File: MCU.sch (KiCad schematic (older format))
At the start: 34 parts, among them Q1 BSS138, SW1 SW_Push, U2 STM32F722RETx

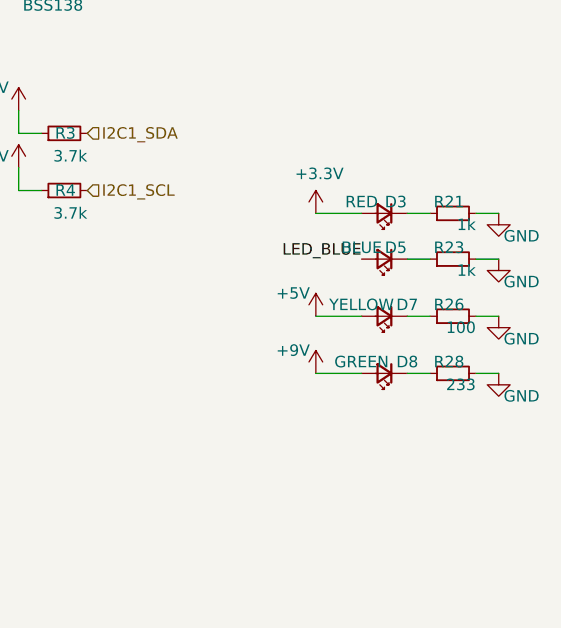
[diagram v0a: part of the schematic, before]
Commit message: Added LED for VCC
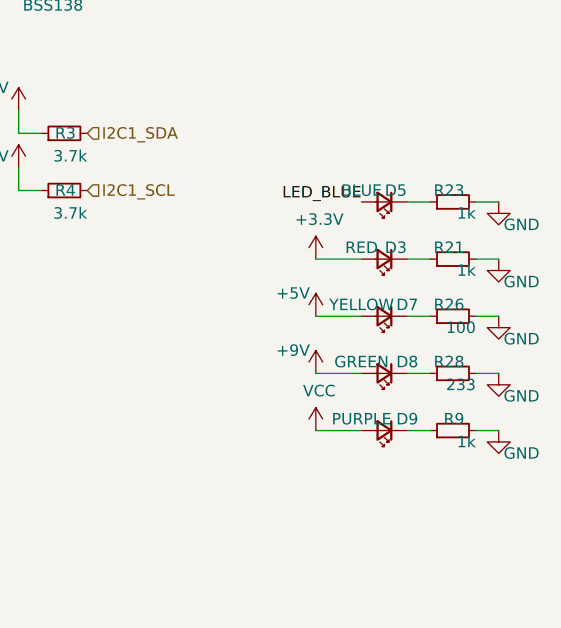
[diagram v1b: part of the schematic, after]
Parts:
- added D9: PURPLE, LED_SMD:LED_0603_1608Metric, symbol Device:LED_Small
- added R9: 1k, Resistor_SMD:R_0402_1005Metric, symbol Device:R_Small
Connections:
- net GND: now also R9.2
- net VCC: now also D9.2 (A)
- new net: D9.1 (K), R9.1
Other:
- moved on the sheet: D3, D5, R21, R23
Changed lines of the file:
@@
 $EndComp
+Wire Wire Line
+	7300 3300 7400 3300
+Wire Wire Line
+	7000 3300 7100 3300
 Wire Wire Line
 	7300 3550 7400 3550
 Wire Wire Line
 	7000 3550 7100 3550
-Wire Wire Line
-	7300 3350 7400 3350
-Wire Wire Line
-	7000 3350 7100 3350
 $Comp
 L power:GND #PWR031
 U 1 1 60863328
+P 7400 3300
+F 0 "#PWR031" H 7400 3050 50  0001 C CNN
+F 1 "GND" H 7500 3200 50  0000 C CNN
+F 2 "" H 7400 3300 50  0001 C CNN
+F 3 "" H 7400 3300 50  0001 C CNN
+	1    7400 3300
+	1    0    0    -1
+$EndComp
+$Comp
+L Device:R_Small R23
+U 1 1 6086332E
+P 7200 3300
+F 0 "R23" V 7250 3250 50  0000 L CNN
+F 1 "1k" V 7150 3200 50  0000 L CNN
+F 2 "Resistor_SMD:R_0402_1005Metric" H 7200 3300 50  0001 C CNN
+F 3 "~" H 7200 3300 50  0001 C CNN
+	1    7200 3300
+	0    -1   -1   0
+$EndComp
+$Comp
+L Device:LED_Small D5
+U 1 1 60863334
+P 6900 3300
+F 0 "D5" H 6850 3250 50  0000 C CNN
+F 1 "BLUE" H 7000 3250 50  0000 C CNN
+F 2 "LED_SMD:LED_0603_1608Metric" V 6900 3300 50  0001 C CNN
+F 3 "~" V 6900 3300 50  0001 C CNN
+	1    6900 3300
+	-1   0    0    1
+$EndComp
+NoConn ~ 4000 4950
+$Comp
+L power:GND #PWR030
+U 1 1 6086335B
 P 7400 3550
-F 0 "#PWR031" H 7400 3300 50  0001 C CNN
+F 0 "#PWR030" H 7400 3300 50  0001 C CNN
 F 1 "GND" H 7500 3450 50  0000 C CNN
 F 2 "" H 7400 3550 50  0001 C CNN
@@
 $EndComp
 $Comp
-L Device:R_Small R23
-U 1 1 6086332E
+L Device:R_Small R21
+U 1 1 60863361
 P 7200 3550
-F 0 "R23" V 7250 3500 50  0000 L CNN
+F 0 "R21" V 7250 3500 50  0000 L CNN
 F 1 "1k" V 7150 3450 50  0000 L CNN
 F 2 "Resistor_SMD:R_0402_1005Metric" H 7200 3550 50  0001 C CNN
@@
 $EndComp
 $Comp
-L Device:LED_Small D5
-U 1 1 60863334
+L Device:LED_Small D3
+U 1 1 60863367
 P 6900 3550
-F 0 "D5" H 6850 3500 50  0000 C CNN
-F 1 "BLUE" H 7000 3500 50  0000 C CNN
+F 0 "D3" H 6850 3500 50  0000 C CNN
+F 1 "RED" H 7000 3500 50  0000 C CNN
 F 2 "LED_SMD:LED_0603_1608Metric" V 6900 3550 50  0001 C CNN
 F 3 "~" V 6900 3550 50  0001 C CNN
 	1    6900 3550
-	-1   0    0    1
-$EndComp
-NoConn ~ 4000 4950
-$Comp
-L power:GND #PWR030
-U 1 1 6086335B
-P 7400 3350
-F 0 "#PWR030" H 7400 3100 50  0001 C CNN
-F 1 "GND" H 7500 3250 50  0000 C CNN
-F 2 "" H 7400 3350 50  0001 C CNN
-F 3 "" H 7400 3350 50  0001 C CNN
-	1    7400 3350
-	1    0    0    -1
-$EndComp
-$Comp
-L Device:R_Small R21
-U 1 1 60863361
-P 7200 3350
-F 0 "R21" V 7250 3300 50  0000 L CNN
-F 1 "1k" V 7150 3250 50  0000 L CNN
-F 2 "Resistor_SMD:R_0402_1005Metric" H 7200 3350 50  0001 C CNN
-F 3 "~" H 7200 3350 50  0001 C CNN
-	1    7200 3350
-	0    -1   -1   0
-$EndComp
-$Comp
-L Device:LED_Small D3
-U 1 1 60863367
-P 6900 3350
-F 0 "D3" H 6850 3300 50  0000 C CNN
-F 1 "RED" H 7000 3300 50  0000 C CNN
-F 2 "LED_SMD:LED_0603_1608Metric" V 6900 3350 50  0001 C CNN
-F 3 "~" V 6900 3350 50  0001 C CNN
-	1    6900 3350
 	-1   0    0    1
 $EndComp
@@
 L power:+3.3V #PWR029
 U 1 1 6086341E
-P 6600 3350
-F 0 "#PWR029" H 6600 3200 50  0001 C CNN
-F 1 "+3.3V" H 6615 3523 50  0000 C CNN
-F 2 "" H 6600 3350 50  0001 C CNN
-F 3 "" H 6600 3350 50  0001 C CNN
-	1    6600 3350
-	1    0    0    -1
-$EndComp
-Wire Wire Line
-	6600 3350 6800 3350
+P 6600 3550
+F 0 "#PWR029" H 6600 3400 50  0001 C CNN
+F 1 "+3.3V" H 6615 3723 50  0000 C CNN
+F 2 "" H 6600 3550 50  0001 C CNN
+F 3 "" H 6600 3550 50  0001 C CNN
+	1    6600 3550
+	1    0    0    -1
+$EndComp
+Wire Wire Line
+	6600 3550 6800 3550
 Connection ~ 3200 5750
 Connection ~ 3300 5750
@@
 Text HLabel 4000 2450 2    50   Input ~ 0
 LED
-Text Label 6800 3550 2    50   ~ 0
+Text Label 6800 3300 2    50   ~ 0
 LED_BLUE
 $Comp
@@
 USB_D+
 NoConn ~ 4000 4850
+Wire Wire Line
+	6600 4300 6800 4300
+Wire Wire Line
+	7300 4300 7400 4300
+Wire Wire Line
+	7000 4300 7100 4300
+$Comp
+L power:GND #PWR0178
+U 1 1 60A4CA89
+P 7400 4300
+F 0 "#PWR0178" H 7400 4050 50  0001 C CNN
+F 1 "GND" H 7500 4200 50  0000 C CNN
+F 2 "" H 7400 4300 50  0001 C CNN
+F 3 "" H 7400 4300 50  0001 C CNN
+	1    7400 4300
+	1    0    0    -1
+$EndComp
+$Comp
+L Device:R_Small R9
+U 1 1 60A4CA8F
+P 7200 4300
+F 0 "R9" V 7250 4250 50  0000 L CNN
+F 1 "1k" V 7150 4200 50  0000 L CNN
+F 2 "Resistor_SMD:R_0402_1005Metric" H 7200 4300 50  0001 C CNN
+F 3 "~" H 7200 4300 50  0001 C CNN
+	1    7200 4300
+	0    -1   -1   0
+$EndComp
+$Comp
+L Device:LED_Small D9
+U 1 1 60A4CA95
+P 6900 4300
+F 0 "D9" H 6800 4250 50  0000 C CNN
+F 1 "PURPLE" H 7000 4250 50  0000 C CNN
+F 2 "LED_SMD:LED_0603_1608Metric" V 6900 4300 50  0001 C CNN
+F 3 "~" V 6900 4300 50  0001 C CNN
+	1    6900 4300
+	-1   0    0    1
+$EndComp
+$Comp
+L power:VCC #PWR0179
+U 1 1 60A4FAC4
+P 6600 4300
+F 0 "#PWR0179" H 6600 4150 50  0001 C CNN
+F 1 "VCC" H 6615 4473 50  0000 C CNN
+F 2 "" H 6600 4300 50  0001 C CNN
+F 3 "" H 6600 4300 50  0001 C CNN
+	1    6600 4300
+	1    0    0    -1
+$EndComp
 $EndSCHEMATC

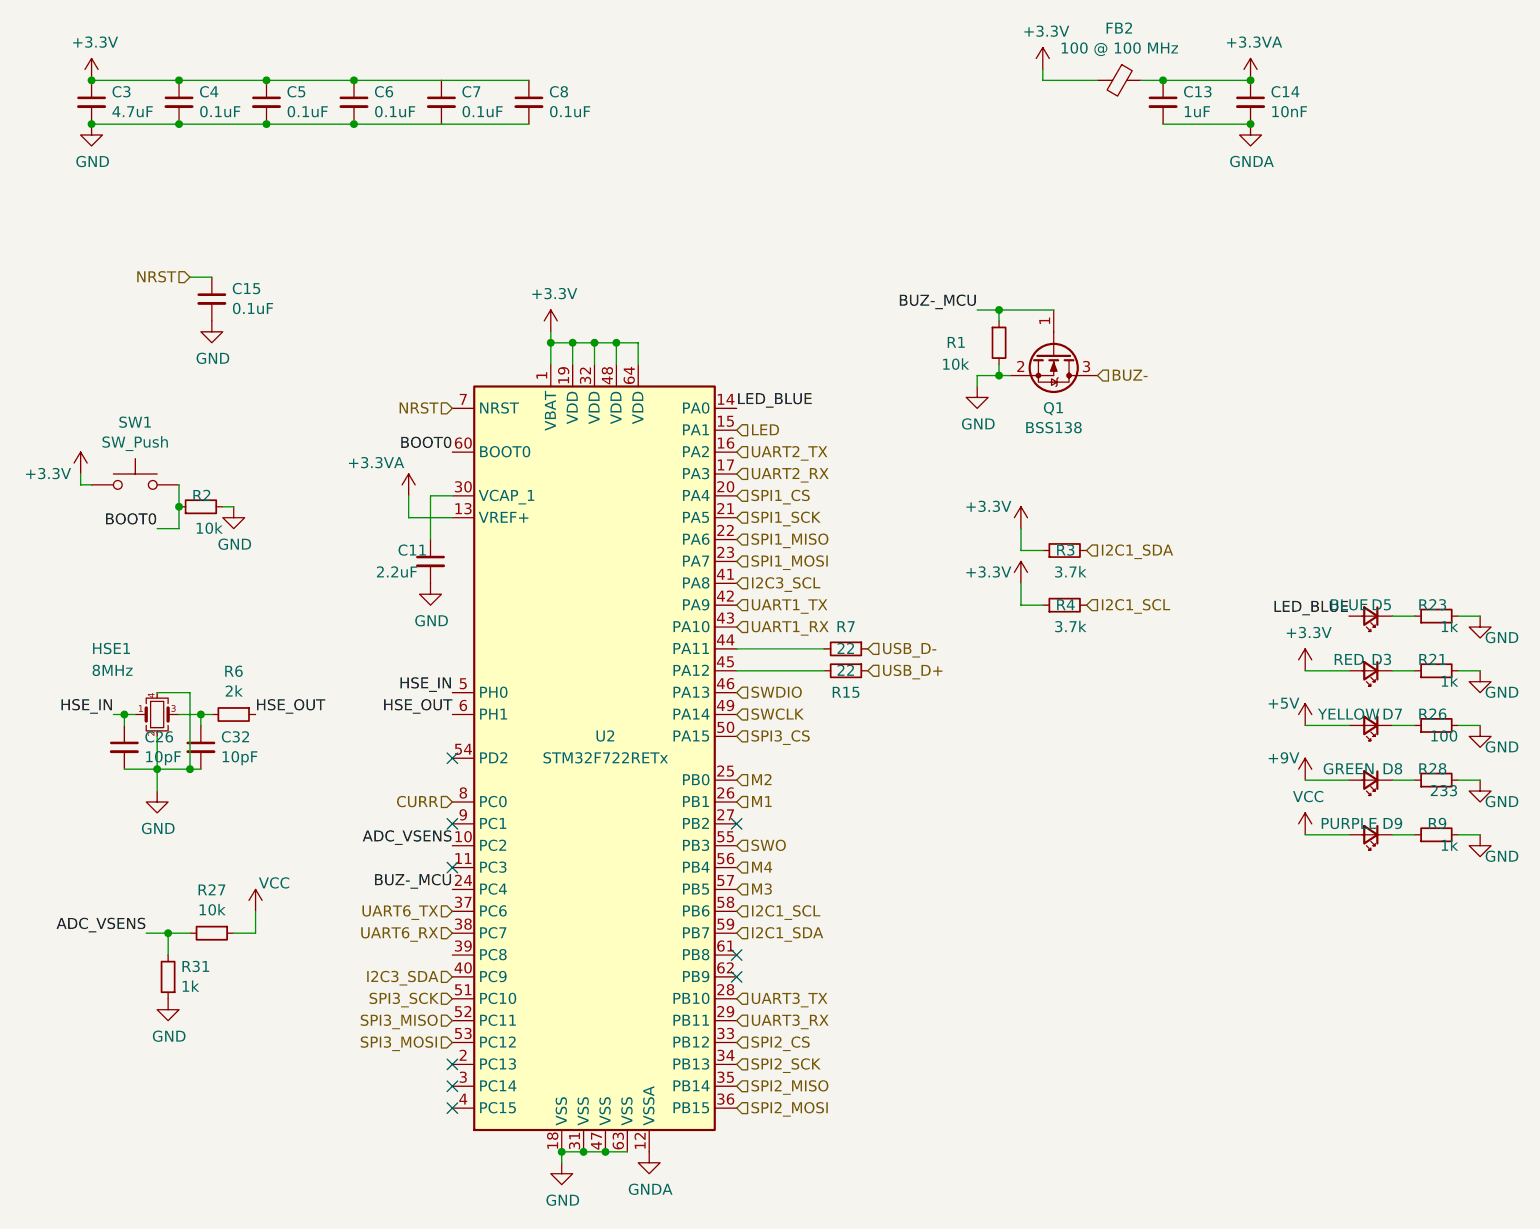
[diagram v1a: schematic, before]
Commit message: Changed to 20x20 form factor
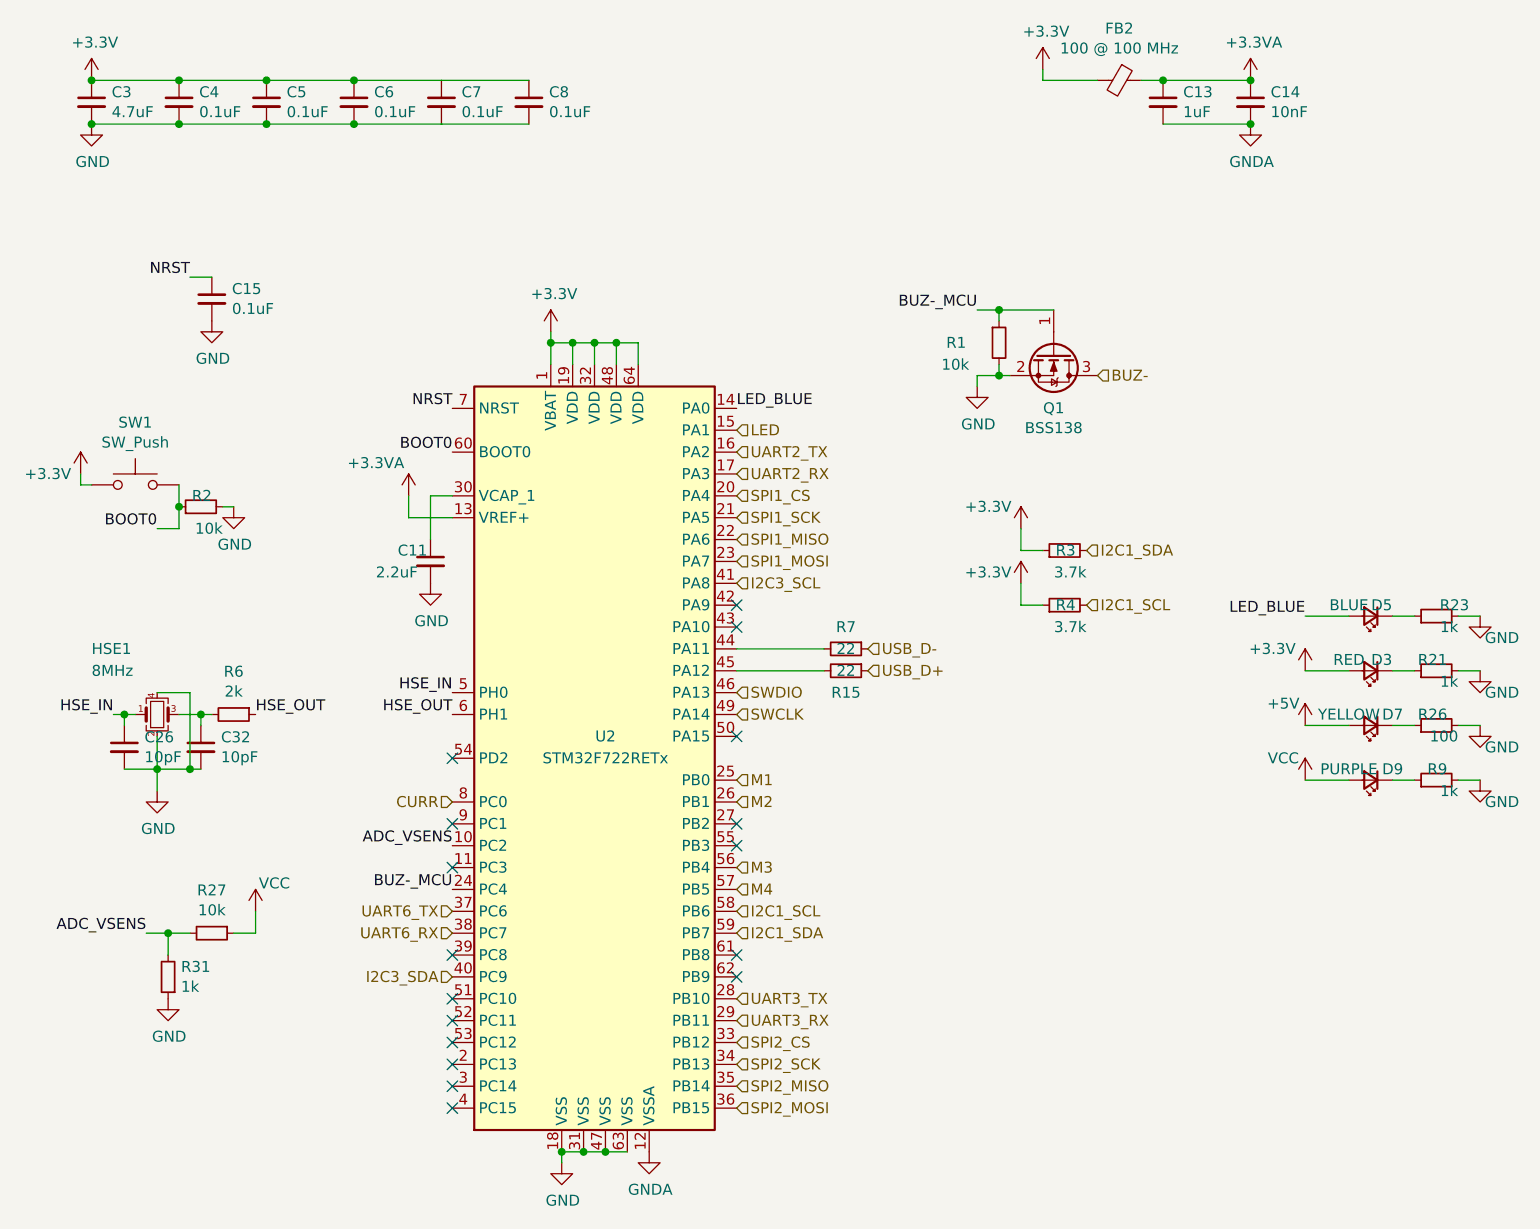
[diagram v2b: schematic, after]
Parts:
- removed D8: GREEN, LED_SMD:LED_0603_1608Metric, symbol Device:LED_Small
- removed R28: 233, Resistor_SMD:R_0402_1005Metric, symbol Device:R_Small
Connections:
- net M1: now also U2.25 (PB0); no longer U2.26 (PB1)
- net M2: now also U2.26 (PB1); no longer U2.25 (PB0)
- net M3: now also U2.56 (PB4); no longer U2.57 (PB5)
- net M4: now also U2.57 (PB5); no longer U2.56 (PB4)
- net SPI3_CS: no longer names the net of U2.50 (PA15)
- net SPI3_MISO: no longer names the net of U2.52 (PC11)
- net SPI3_MOSI: no longer names the net of U2.53 (PC12)
- net SPI3_SCK: no longer names the net of U2.51 (PC10)
- net SWO: no longer names the net of U2.55 (PB3)
- net UART1_RX: no longer names the net of U2.43 (PA10)
- net UART1_TX: no longer names the net of U2.42 (PA9)
- no-connect marks 9 -> 17
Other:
- moved on the sheet: D9, R9
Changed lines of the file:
@@
 $Descr A4 11693 8268
 encoding utf-8
-Sheet 2 8
+Sheet 2 7
 Title ""
 Date ""
@@
 $EndComp
 Wire Wire Line
-	6600 4050 6800 4050
-Wire Wire Line
-	7300 4050 7400 4050
-Wire Wire Line
-	7000 4050 7100 4050
-$Comp
-L power:GND #PWR041
-U 1 1 608631CC
-P 7400 4050
-F 0 "#PWR041" H 7400 3800 50  0001 C CNN
-F 1 "GND" H 7500 3950 50  0000 C CNN
-F 2 "" H 7400 4050 50  0001 C CNN
-F 3 "" H 7400 4050 50  0001 C CNN
-	1    7400 4050
-	1    0    0    -1
-$EndComp
-$Comp
-L Device:R_Small R28
-U 1 1 608631D2
-P 7200 4050
-F 0 "R28" V 7250 4000 50  0000 L CNN
-F 1 "233" V 7150 3950 50  0000 L CNN
-F 2 "Resistor_SMD:R_0402_1005Metric" H 7200 4050 50  0001 C CNN
-F 3 "~" H 7200 4050 50  0001 C CNN
-	1    7200 4050
-	0    -1   -1   0
-$EndComp
-$Comp
-L Device:LED_Small D8
-U 1 1 608631D8
-P 6900 4050
-F 0 "D8" H 6800 4000 50  0000 C CNN
-F 1 "GREEN" H 7000 4000 50  0000 C CNN
-F 2 "LED_SMD:LED_0603_1608Metric" V 6900 4050 50  0001 C CNN
-F 3 "~" V 6900 4050 50  0001 C CNN
-	1    6900 4050
-	-1   0    0    1
-$EndComp
-$Comp
-L power:+9V #PWR037
-U 1 1 608631DE
-P 6600 4050
-F 0 "#PWR037" H 6600 3900 50  0001 C CNN
-F 1 "+9V" H 6500 4150 50  0000 C CNN
-F 2 "" H 6600 4050 50  0001 C CNN
-F 3 "" H 6600 4050 50  0001 C CNN
-	1    6600 4050
-	1    0    0    -1
-$EndComp
-Wire Wire Line
 	6600 3800 6800 3800
 Wire Wire Line
@@
 U 1 1 6086332E
 P 7200 3300
-F 0 "R23" V 7250 3250 50  0000 L CNN
+F 0 "R23" V 7250 3150 50  0000 L CNN
 F 1 "1k" V 7150 3200 50  0000 L CNN
 F 2 "Resistor_SMD:R_0402_1005Metric" H 7200 3300 50  0001 C CNN
@@
 P 6600 3550
 F 0 "#PWR029" H 6600 3400 50  0001 C CNN
-F 1 "+3.3V" H 6615 3723 50  0000 C CNN
+F 1 "+3.3V" H 6450 3650 50  0000 C CNN
 F 2 "" H 6600 3550 50  0001 C CNN
 F 3 "" H 6600 3550 50  0001 C CNN
@@
 Text HLabel 4000 2650 2    50   Input ~ 0
 UART2_RX
-Text HLabel 4000 4150 2    50   Input ~ 0
+Text HLabel 4000 4050 2    50   Input ~ 0
 M1
 Text HLabel 4000 3150 2    50   Input ~ 0
 I2C3_SCL
-Text HLabel 4000 3250 2    50   Input ~ 0
-UART1_TX
-Text HLabel 4000 3350 2    50   Input ~ 0
-UART1_RX
 Wire Wire Line
 	4400 3450 4000 3450
@@
 Text HLabel 4000 3750 2    50   Input ~ 0
 SWCLK
-Text HLabel 4000 3850 2    50   Input ~ 0
-SPI3_CS
+Text HLabel 4000 4550 2    50   Input ~ 0
+M4
 Text HLabel 4000 4450 2    50   Input ~ 0
-M4
-Text HLabel 4000 4550 2    50   Input ~ 0
 M3
-Text HLabel 4000 4350 2    50   Input ~ 0
-SWO
 Text Label 4000 2350 0    50   ~ 0
 LED_BLUE
@@
 Text HLabel 4000 5550 2    50   Input ~ 0
 SPI2_MOSI
-Text HLabel 2700 5250 0    50   Input ~ 0
-SPI3_MOSI
-Text HLabel 2700 5150 0    50   Input ~ 0
-SPI3_MISO
-Text HLabel 2700 5050 0    50   Input ~ 0
-SPI3_SCK
 Text HLabel 2700 4950 0    50   Input ~ 0
 I2C3_SDA
-Text HLabel 4000 4050 2    50   Input ~ 0
+Text HLabel 4000 4150 2    50   Input ~ 0
 M2
 Text HLabel 2700 4750 0    50   Input ~ 0
@@
 Text HLabel 5600 3000 2    50   Input ~ 0
 I2C1_SDA
-Text HLabel 2700 2350 0    50   Input ~ 0
-NRST
-Text HLabel 1500 1750 0    50   Input ~ 0
-NRST
 Wire Wire Line
 	1350 4000 1500 4000
@@
 Text HLabel 4000 2450 2    50   Input ~ 0
 LED
-Text Label 6800 3300 2    50   ~ 0
+Text Label 6600 3300 2    50   ~ 0
 LED_BLUE
 $Comp
@@
 NoConn ~ 4000 4850
 Wire Wire Line
-	6600 4300 6800 4300
-Wire Wire Line
-	7300 4300 7400 4300
-Wire Wire Line
-	7000 4300 7100 4300
+	6600 4050 6800 4050
+Wire Wire Line
+	7300 4050 7400 4050
+Wire Wire Line
+	7000 4050 7100 4050
 $Comp
 L power:GND #PWR0178
 U 1 1 60A4CA89
-P 7400 4300
-F 0 "#PWR0178" H 7400 4050 50  0001 C CNN
-F 1 "GND" H 7500 4200 50  0000 C CNN
-F 2 "" H 7400 4300 50  0001 C CNN
-F 3 "" H 7400 4300 50  0001 C CNN
-	1    7400 4300
+P 7400 4050
+F 0 "#PWR0178" H 7400 3800 50  0001 C CNN
+F 1 "GND" H 7500 3950 50  0000 C CNN
+F 2 "" H 7400 4050 50  0001 C CNN
+F 3 "" H 7400 4050 50  0001 C CNN
+	1    7400 4050
 	1    0    0    -1
 $EndComp
@@
 L Device:R_Small R9
 U 1 1 60A4CA8F
-P 7200 4300
-F 0 "R9" V 7250 4250 50  0000 L CNN
-F 1 "1k" V 7150 4200 50  0000 L CNN
-F 2 "Resistor_SMD:R_0402_1005Metric" H 7200 4300 50  0001 C CNN
-F 3 "~" H 7200 4300 50  0001 C CNN
-	1    7200 4300
+P 7200 4050
+F 0 "R9" V 7250 4000 50  0000 L CNN
+F 1 "1k" V 7150 3950 50  0000 L CNN
+F 2 "Resistor_SMD:R_0402_1005Metric" H 7200 4050 50  0001 C CNN
+F 3 "~" H 7200 4050 50  0001 C CNN
+	1    7200 4050
 	0    -1   -1   0
 $EndComp
@@
 L Device:LED_Small D9
 U 1 1 60A4CA95
-P 6900 4300
-F 0 "D9" H 6800 4250 50  0000 C CNN
-F 1 "PURPLE" H 7000 4250 50  0000 C CNN
-F 2 "LED_SMD:LED_0603_1608Metric" V 6900 4300 50  0001 C CNN
-F 3 "~" V 6900 4300 50  0001 C CNN
-	1    6900 4300
+P 6900 4050
+F 0 "D9" H 6800 4000 50  0000 C CNN
+F 1 "PURPLE" H 7000 4000 50  0000 C CNN
+F 2 "LED_SMD:LED_0603_1608Metric" V 6900 4050 50  0001 C CNN
+F 3 "~" V 6900 4050 50  0001 C CNN
+	1    6900 4050
 	-1   0    0    1
 $EndComp
@@
 L power:VCC #PWR0179
 U 1 1 60A4FAC4
-P 6600 4300
-F 0 "#PWR0179" H 6600 4150 50  0001 C CNN
-F 1 "VCC" H 6615 4473 50  0000 C CNN
-F 2 "" H 6600 4300 50  0001 C CNN
-F 3 "" H 6600 4300 50  0001 C CNN
-	1    6600 4300
-	1    0    0    -1
-$EndComp
+P 6600 4050
+F 0 "#PWR0179" H 6600 3900 50  0001 C CNN
+F 1 "VCC" H 6500 4150 50  0000 C CNN
+F 2 "" H 6600 4050 50  0001 C CNN
+F 3 "" H 6600 4050 50  0001 C CNN
+	1    6600 4050
+	1    0    0    -1
+$EndComp
+NoConn ~ 4000 3850
+NoConn ~ 2700 5250
+NoConn ~ 2700 5150
+NoConn ~ 2700 5050
+NoConn ~ 2700 4850
+Wire Wire Line
+	6600 3300 6800 3300
+NoConn ~ 4000 4350
+Text Label 2700 2350 2    50   ~ 0
+NRST
+Text Label 1500 1750 2    50   ~ 0
+NRST
+NoConn ~ 4000 3250
+NoConn ~ 4000 3350
 $EndSCHEMATC
